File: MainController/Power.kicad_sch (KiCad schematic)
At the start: 0 parts

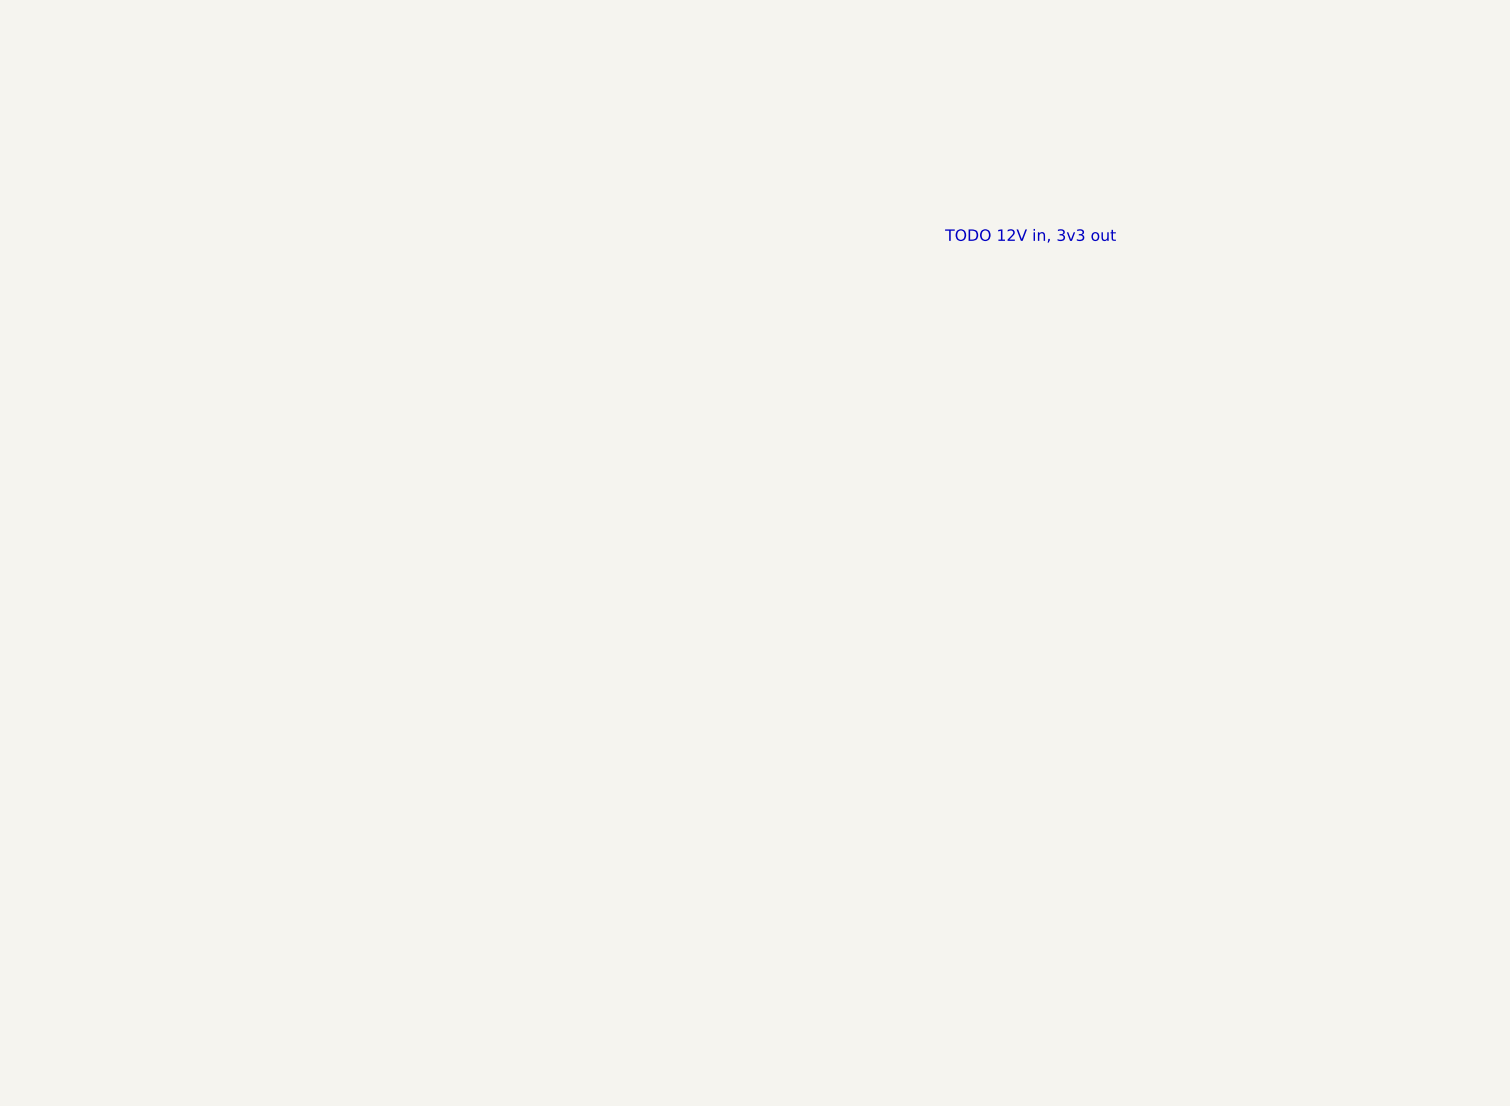
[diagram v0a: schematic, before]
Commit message: WIP - Starting Voltage Measurement
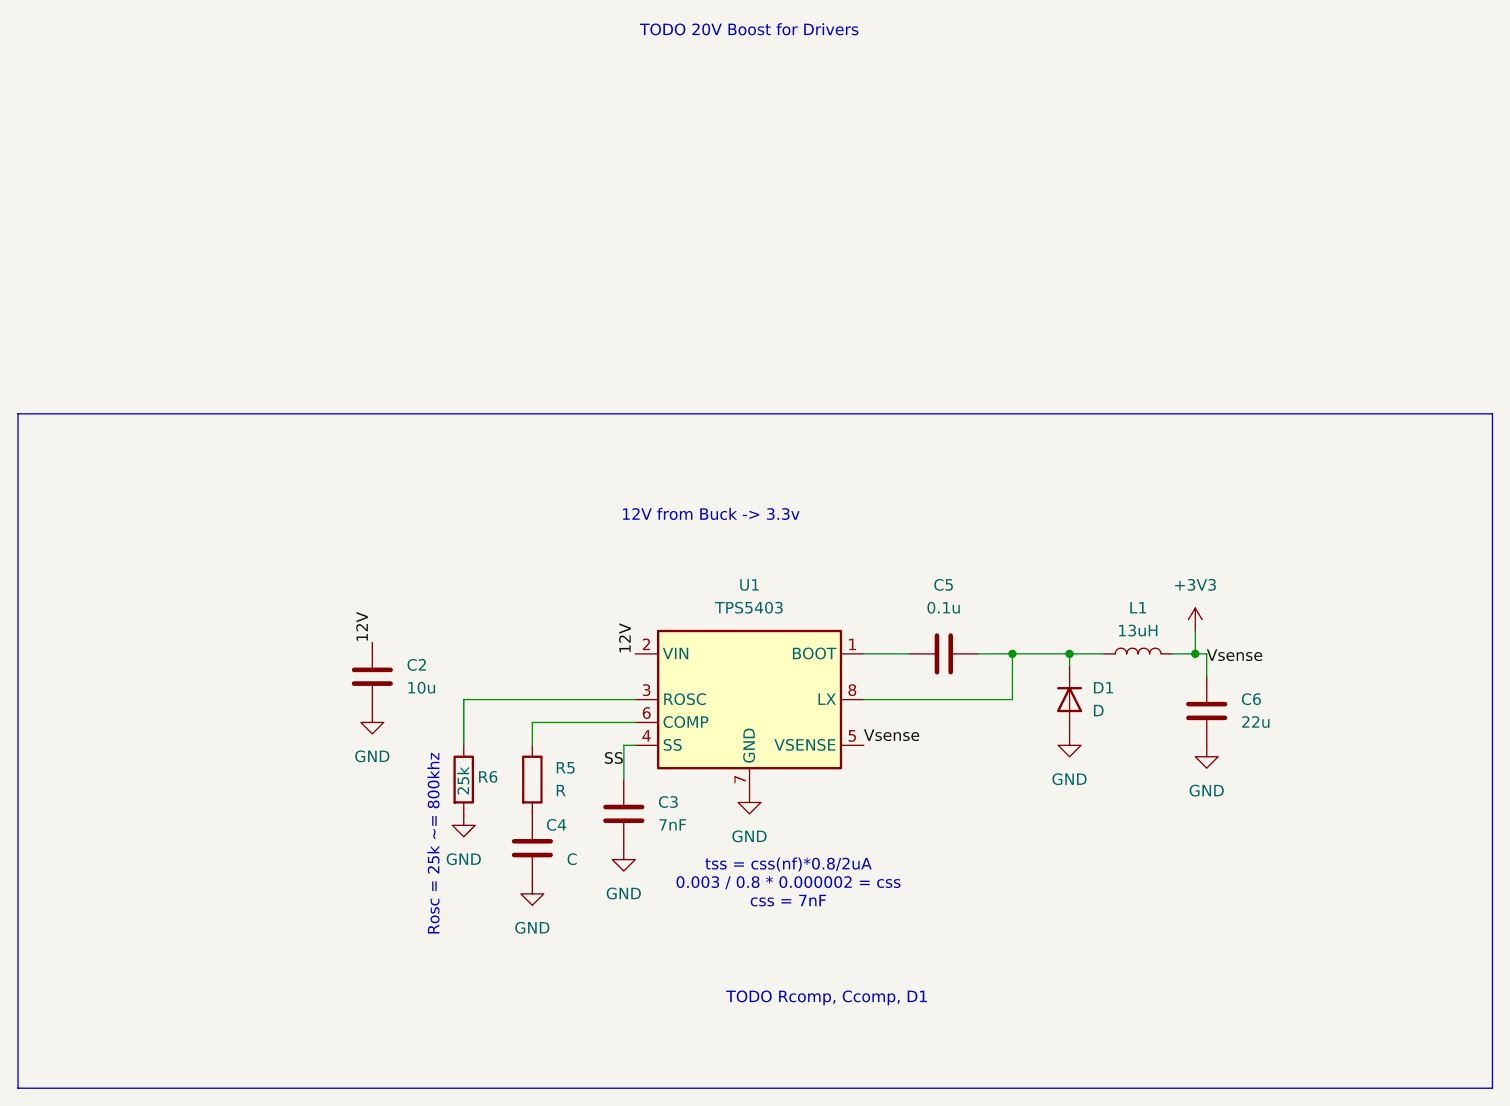
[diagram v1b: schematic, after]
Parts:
- added C2: 10u, Capacitor_SMD:C_0805_2012Metric_Pad1.18x1.45mm_HandSolder, symbol Device:C
- added C3: 7nF, Capacitor_SMD:C_0402_1005Metric_Pad0.74x0.62mm_HandSolder, symbol Device:C
- added C4: C, symbol Device:C
- added C5: 0.1u, Capacitor_SMD:C_0402_1005Metric_Pad0.74x0.62mm_HandSolder, symbol Device:C
- added C6: 22u, Capacitor_SMD:C_0805_2012Metric_Pad1.18x1.45mm_HandSolder, symbol Device:C
- added D1: D, symbol Device:D
- added L1: 13uH, symbol Device:L
- added R5: R, symbol Device:R
- added R6: 25k, Resistor_SMD:R_0402_1005Metric_Pad0.72x0.64mm_HandSolder, symbol Device:R
- added U1: TPS5403, Package_SO:SOIC-8_3.9x4.9mm_P1.27mm, symbol Regulator_Switching:TPS5403
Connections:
- new net: C5.1, U1.1 (BOOT)
- new net: R6.1, U1.3 (ROSC)
- new net: R5.1, U1.6 (COMP)
- new net: C5.2, D1.1 (K), L1.1, U1.8 (LX)
- new net: C4.1, R5.2
- new net +3V3: C6.1, L1.2, U1.5 (VSENSE)
- new net 12V: C2.1, U1.2 (VIN)
- new net GND: C2.2, C3.2, C4.2, C6.2, D1.2 (A), R6.2, U1.7 (GND)
- new net SS: C3.1, U1.4 (SS)
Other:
- note added: "12V from Buck -> 3.3v"
- note added: "Rosc = 25k ~= 800khz"
- note added: "TODO 20V Boost for Drivers"
- note added: "TODO Rcomp, Ccomp, D1"
- note added: "tss = css(nf)*0.8/2uA 0.003 / 0.8 * 0.000002 = css css = 7nF"
- note removed: "TODO 12V in, 3v3 out"

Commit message: WIP - HV measurement may be done
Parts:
- added C10: 1u, symbol Device:C
- added C8: 0.1u, Capacitor_SMD:C_0402_1005Metric_Pad0.74x0.62mm_HandSolder, symbol Device:C
- added C9: 1u, Capacitor_SMD:C_0402_1005Metric_Pad0.74x0.62mm_HandSolder, symbol Device:C
- added D2, D3: D_Schottky, Diode_SMD:D_0603_1608Metric_Pad1.05x0.95mm_HandSolder, symbol Device:D_Schottky
- added TR1: Txformer, symbol Transformer:ADTT1-1
- added U3: ~, symbol New_Library:SN6501-Q1
- D1: footprint (none) -> Diode_SMD:D_0603_1608Metric_Pad1.05x0.95mm_HandSolder
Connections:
- net +3V3: now also C8.1, C9.1, TR1.2, U3.2 (VCC)
- net GND: now also C8.2, C9.2, U3.4 (GND), U3.5 (GND)
- new net: D3.2 (A), TR1.4
- new net: D2.2 (A), TR1.6
- new net 3v3_iso: C10.1, D2.1 (K), D3.1 (K)
- new net D1: TR1.1, U3.1 (D1)
- new net D2: TR1.3, U3.3 (D2)
- new net GND1: C10.2, TR1.5
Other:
- note added: "TODO this looks right? Confirm"
- moved on the sheet: C2, C3, C4, C5, C6, D1, L1, R5, R6, U1
